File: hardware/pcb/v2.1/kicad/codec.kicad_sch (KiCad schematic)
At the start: 22 parts, among them U1 TLV320AIC3104IRHBR, U2 XC6206P182MR

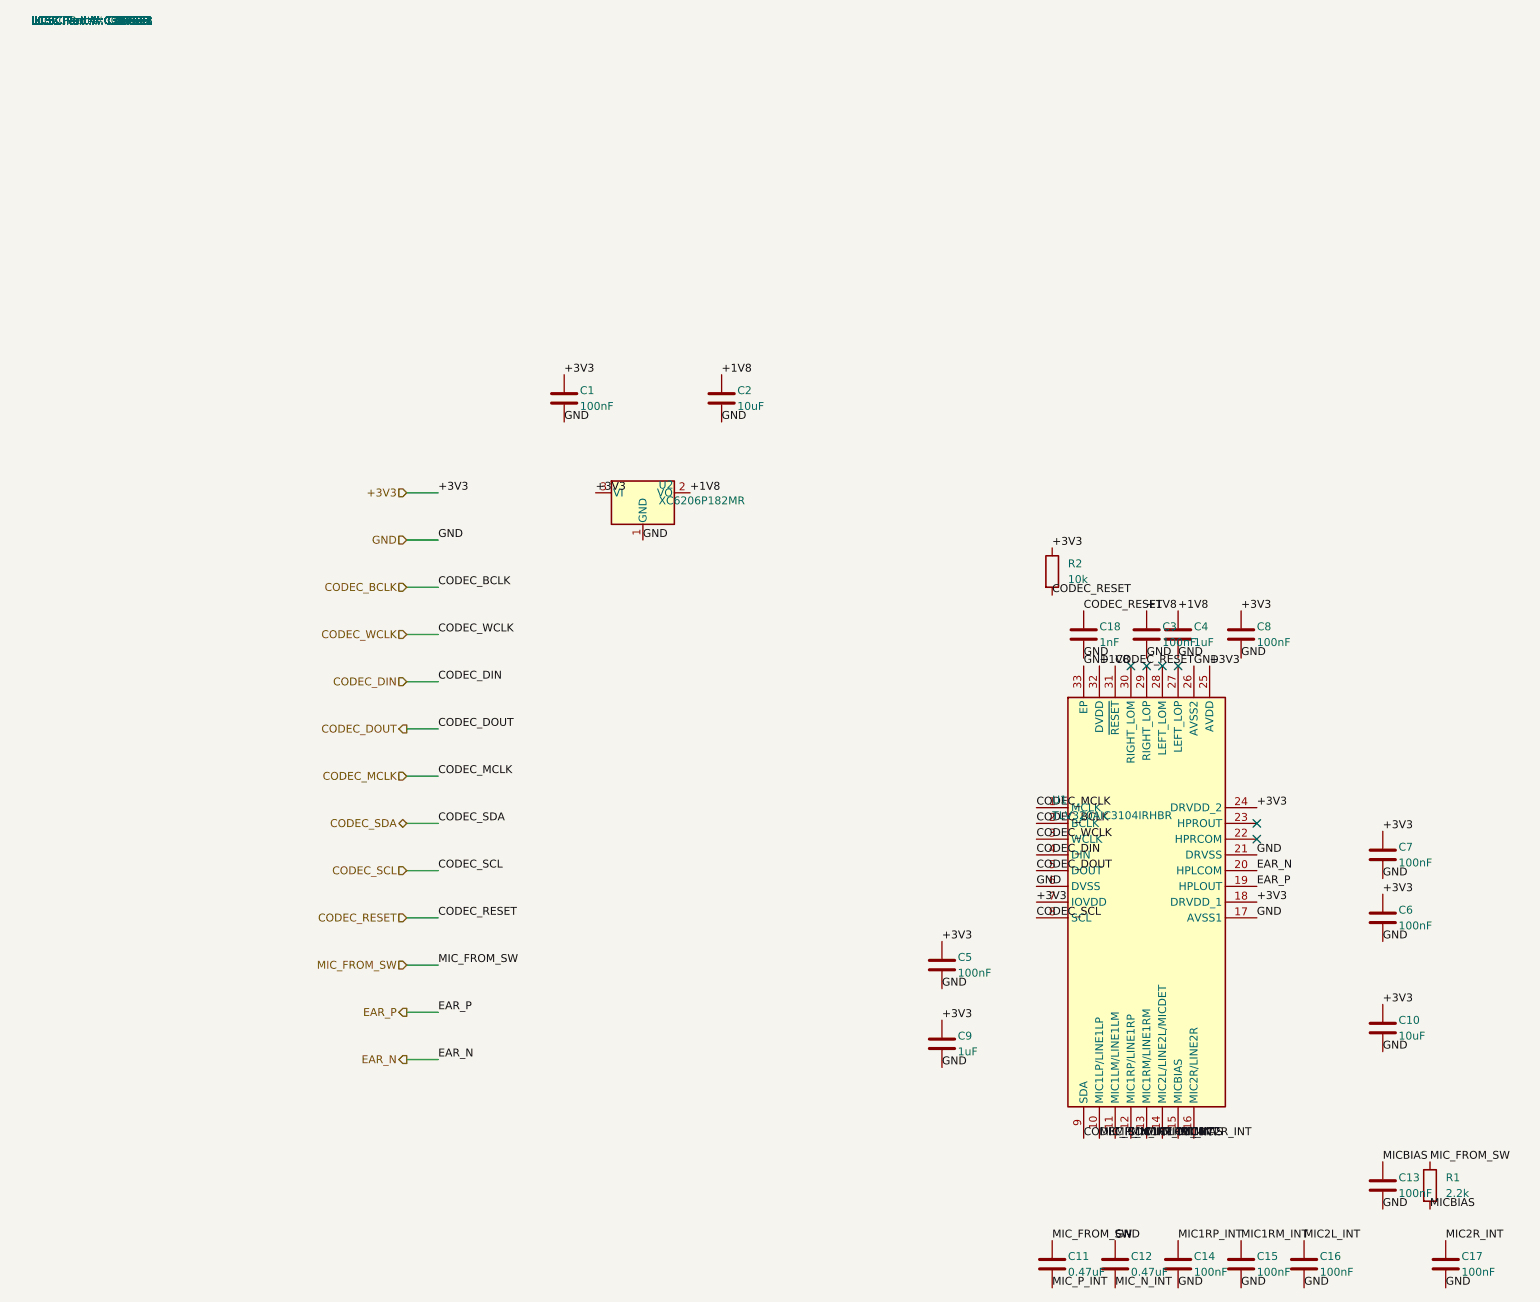
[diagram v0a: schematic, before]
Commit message: feat(hardware): switch to 5V input, drop buck stage, retarget boost to 37V
Bench testing confirmed the on-board boost approach matches the external
transformer for bell loudness: 79 dBA (transformer) vs 78 dBA (boost at 33V),
measured same distance/room/meter. The transformer is no longer justified.

Power input changed from 12V to 5V:
- Removed the entire LM2596 buck stage (U1, L1, D1, C2, C56). With 5V input
  there is nothing to buck down for the Pi; 5V feeds the Pi, the AMS1117 LDO,
  and the XL6019 boost directly.
- Merged the old +12V rail into +5V throughout both sheets.
- J3 connector kept as-is for now (barrel-jack pigtail); it will need a
  higher-current part since 5V at the same power draws ~2x the current.
- R12 (12V power LED resistor) changed 1k -> 300R to rebias for the 5V rail.

Boost output retargeted 42V -> 37V (R20 64.9k -> 57.6k, R21 unchanged at 2k):
- 37V gives 8V margin below the DRV8871's 45V VM limit (was only 3V at 42V).
- Bell already measured 78 dBA at 33V; 37V is marginally louder with far
  better headroom against inductive-kickback spikes.
- Lower boost ratio is also easier on the XL6019 from a 5V input.

PCB: boost cluster (U10/L10/D10/C100/C101/R20/R21) repositioned from the
off-board scratch area into the region between U2 and the codec. All
footprints on F.Cu. Layout and routing still in progress.

ERC clean (0 errors). Netlist: 77 components, +12V net fully eliminated,
codec subsheet intact (22 components).
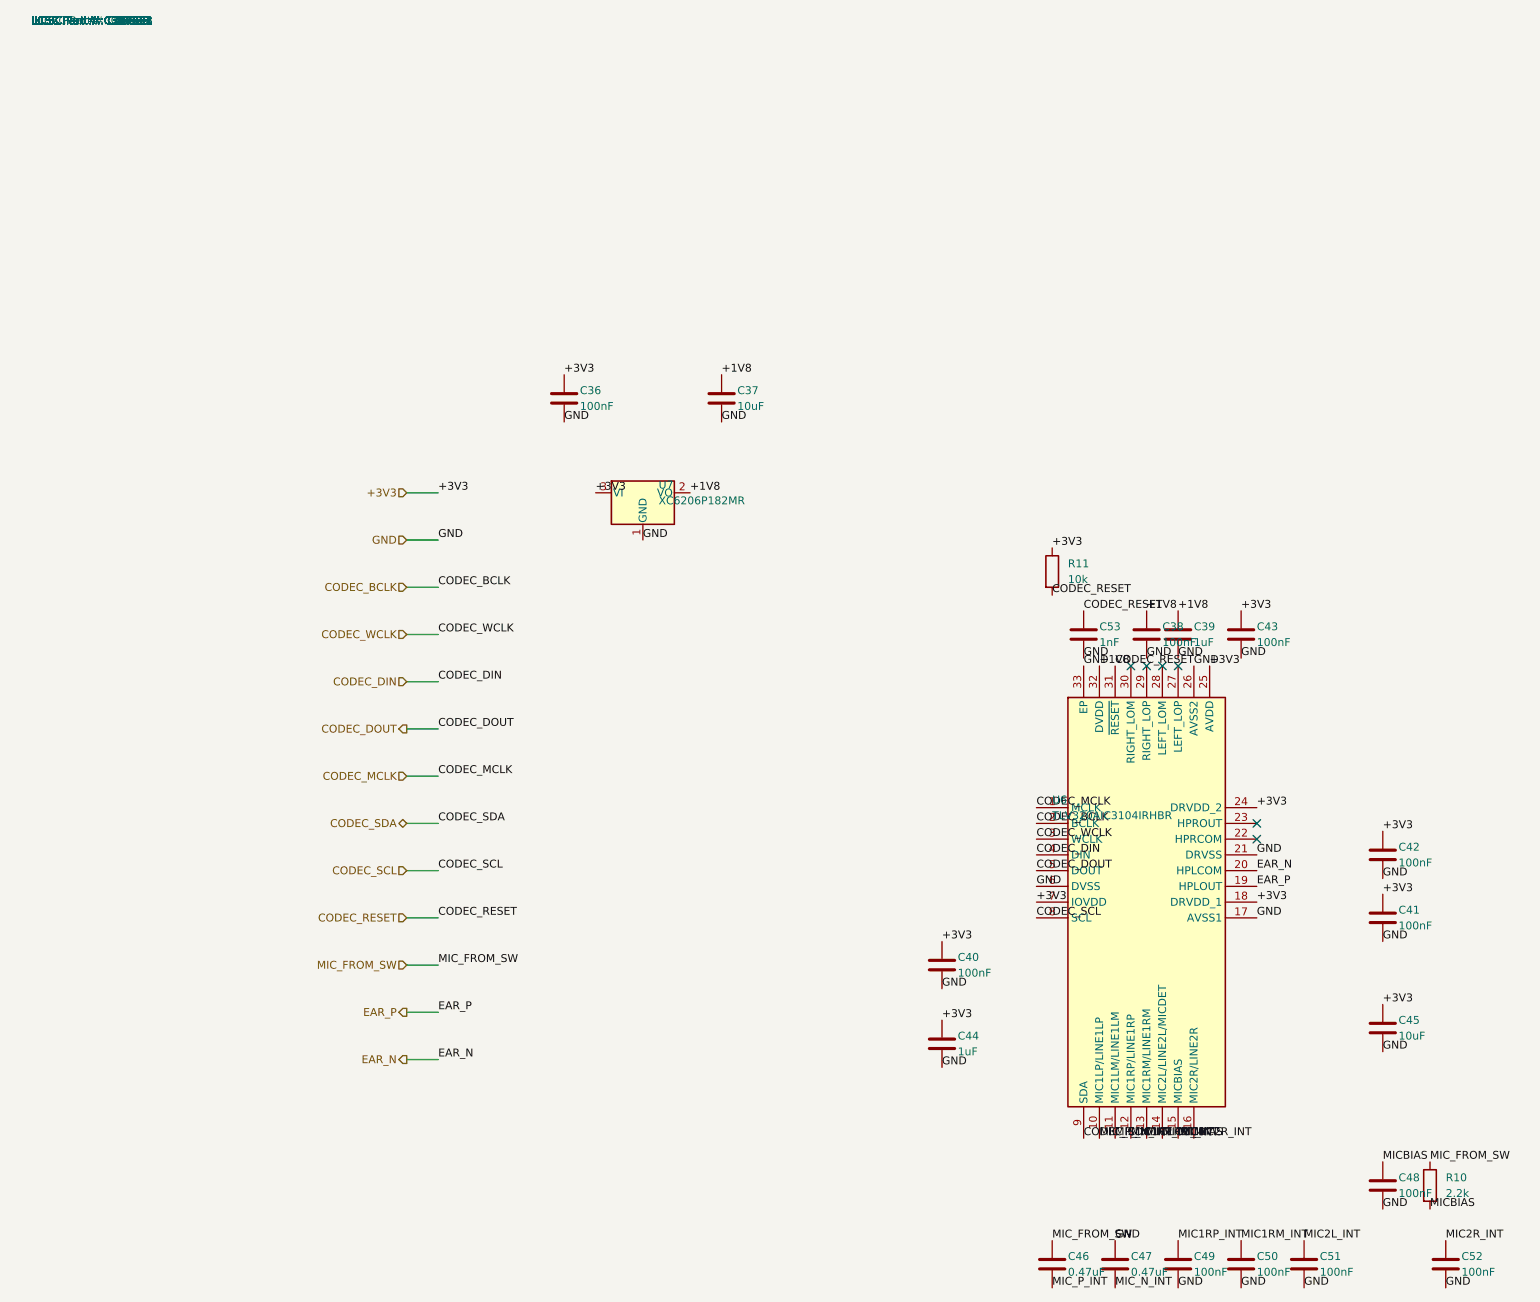
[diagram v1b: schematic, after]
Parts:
- renumbered C1 to C36, C2 to C37, C3 to C38, C4 to C39, C5 to C40, C6 to C41, C7 to C42, C8 to C43, C9 to C44, C10 to C45, C11 to C46, C12 to C47, C13 to C48, C14 to C49, C15 to C50, C16 to C51, C17 to C52, C18 to C53, R1 to R10, R2 to R11, U1 to U6, U2 to U7
